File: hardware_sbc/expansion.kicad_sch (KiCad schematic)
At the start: 5 parts, among them J11 DF40HC(3.5)-60DS, J12 DF40HC(3.5)-60DS, U1 IMX8MM, U1H IMX8MM, U1J IMX8MM

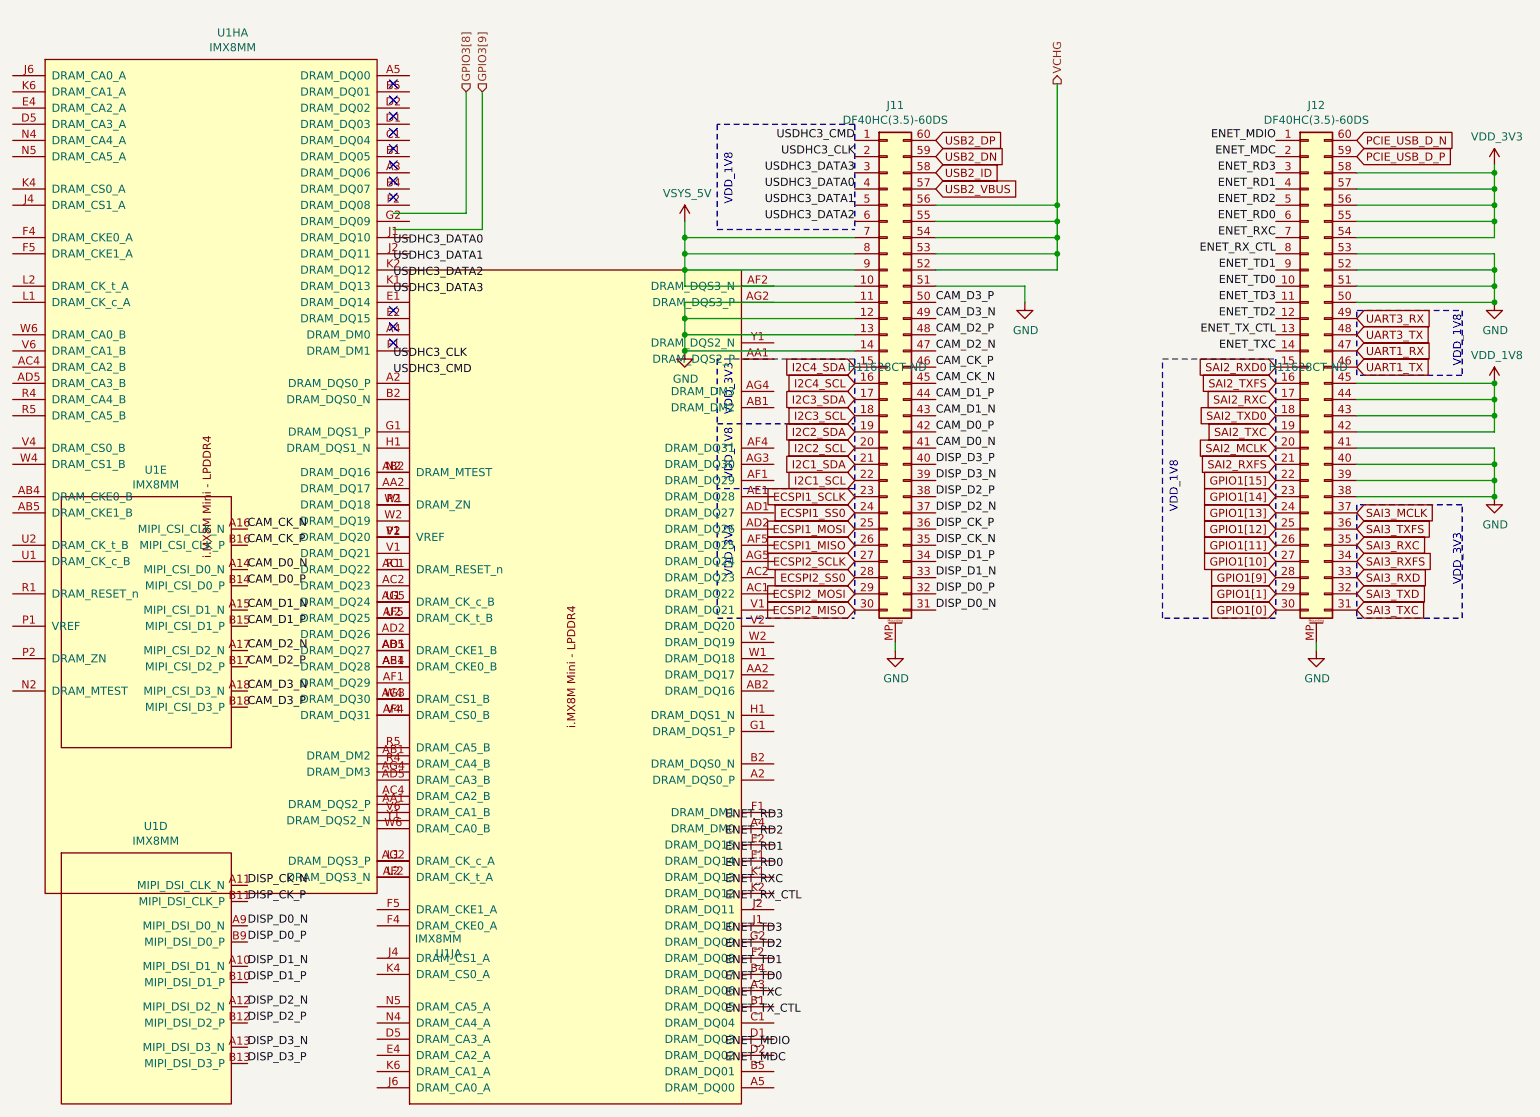
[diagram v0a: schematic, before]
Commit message: Updated production files and fixed schematic link issue.
Fixed schematic unit number issue and re-linked to PCB.
New gerbers, STEP file, schematic PDF.
Deleted old KiCAD 6 files.
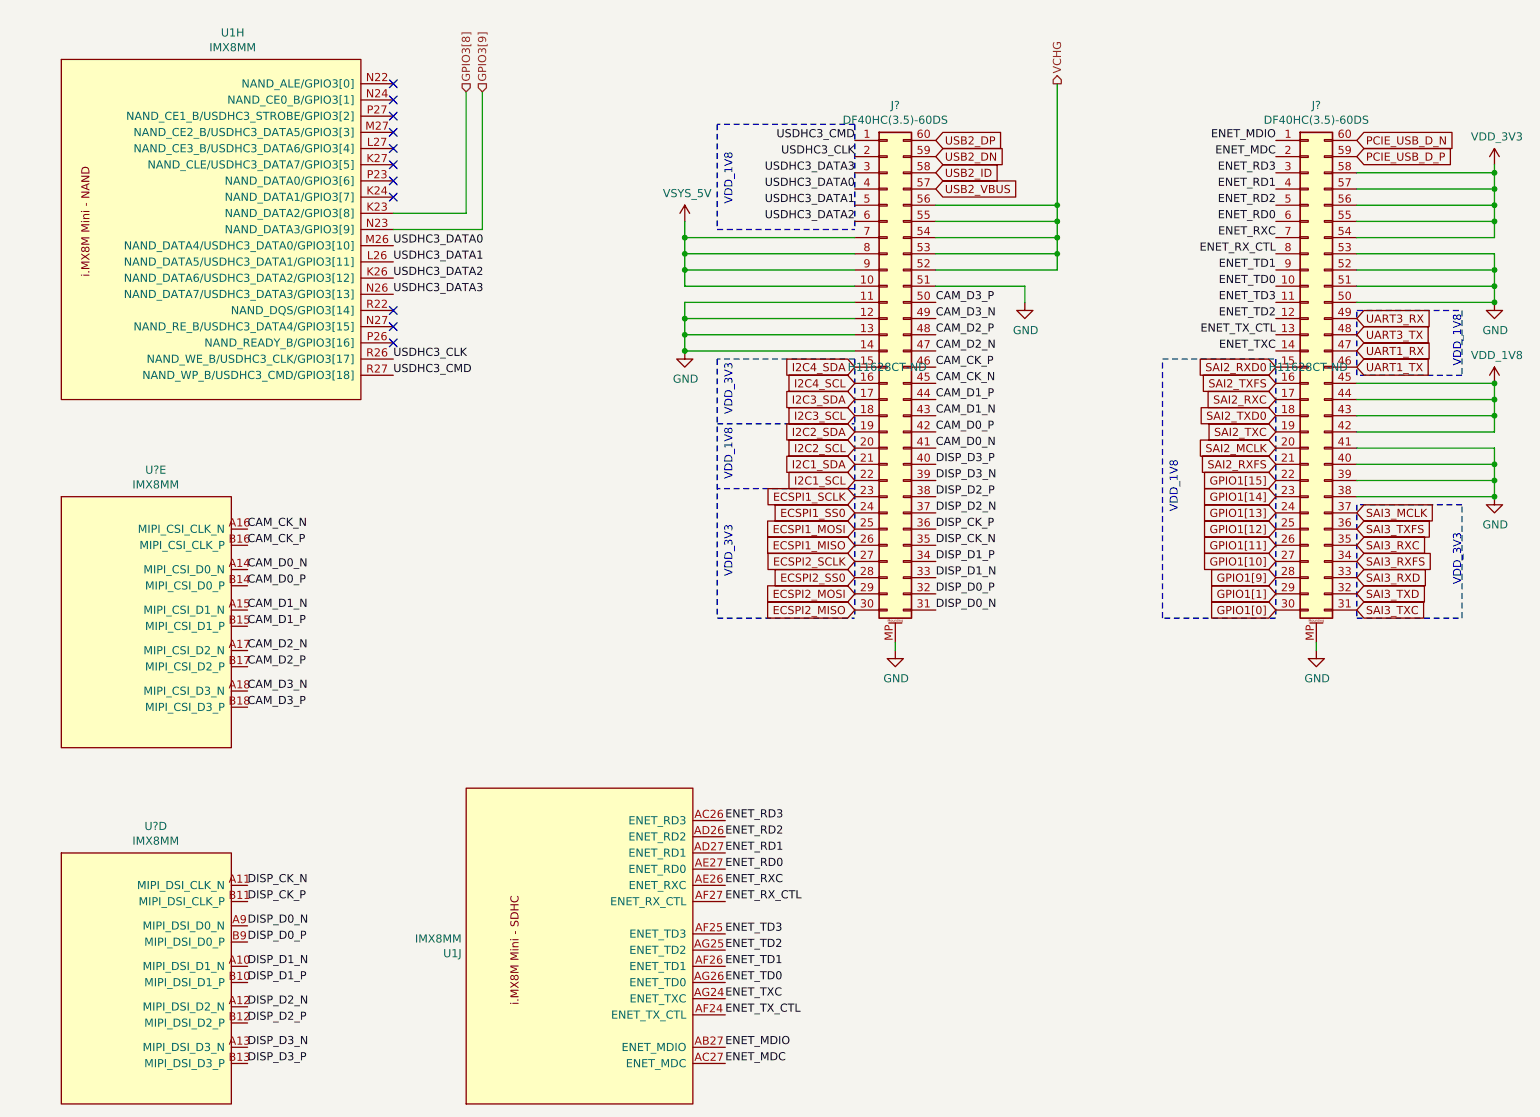
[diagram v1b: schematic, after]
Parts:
- renumbered J11 to J?, J12 to J?, U1H to U1, U1J to U1, U1 to U?
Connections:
- net ENET_MDC: now also U1.AC27 (ENET_MDC)
- net ENET_MDIO: now also U1.AB27 (ENET_MDIO)
- net ENET_RD0: now also U1.AE27 (ENET_RD0)
- net ENET_RD1: now also U1.AD27 (ENET_RD1)
- net ENET_RD2: now also U1.AD26 (ENET_RD2)
- net ENET_RD3: now also U1.AC26 (ENET_RD3)
- net ENET_RXC: now also U1.AE26 (ENET_RXC)
- net ENET_RX_CTL: now also U1.AF27 (ENET_RX_CTL)
- net ENET_TD0: now also U1.AG26 (ENET_TD0)
- net ENET_TD1: now also U1.AF26 (ENET_TD1)
- net ENET_TD2: now also U1.AG25 (ENET_TD2)
- net ENET_TD3: now also U1.AF25 (ENET_TD3)
- net ENET_TXC: now also U1.AG24 (ENET_TXC)
- net ENET_TX_CTL: now also U1.AF24 (ENET_TX_CTL)
- net GPIO3[8]: now also U1.K23 (NAND_DATA2/GPIO3[8])
- net GPIO3[9]: now also U1.N23 (NAND_DATA3/GPIO3[9])
- net USDHC3_CLK: now also U1.R26 (NAND_WE_B/USDHC3_CLK/GPIO3[17])
- net USDHC3_CMD: now also U1.R27 (NAND_WP_B/USDHC3_CMD/GPIO3[18])
- net USDHC3_DATA0: now also U1.M26 (NAND_DATA4/USDHC3_DATA0/GPIO3[10])
- net USDHC3_DATA1: now also U1.L26 (NAND_DATA5/USDHC3_DATA1/GPIO3[11])
- net USDHC3_DATA2: now also U1.K26 (NAND_DATA6/USDHC3_DATA2/GPIO3[12])
- net USDHC3_DATA3: now also U1.N26 (NAND_DATA7/USDHC3_DATA3/GPIO3[13])
